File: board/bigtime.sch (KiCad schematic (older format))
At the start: 61 parts, among them IC1 NPIC6C596A, IC2 TPS62152, IC3 25AA02E48, IC4 STM32F407VET6, IC8 LDL212DR, J2 MICROUSB, P1 CONN_IN, P2 CONN_OUT, P3 +12V, P4 SWD_TC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

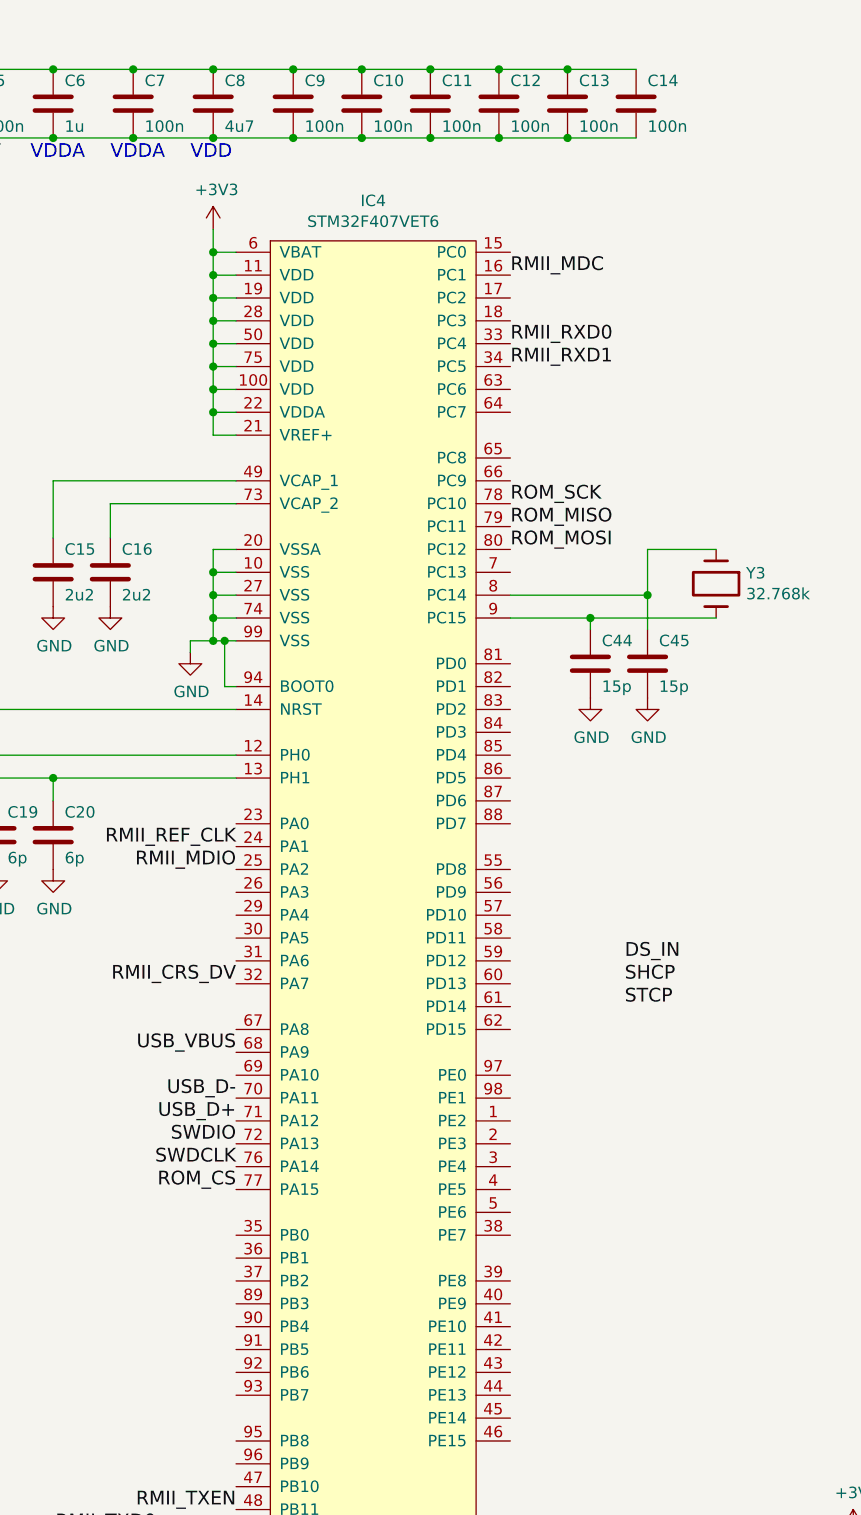
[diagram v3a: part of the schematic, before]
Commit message: nearly done first route
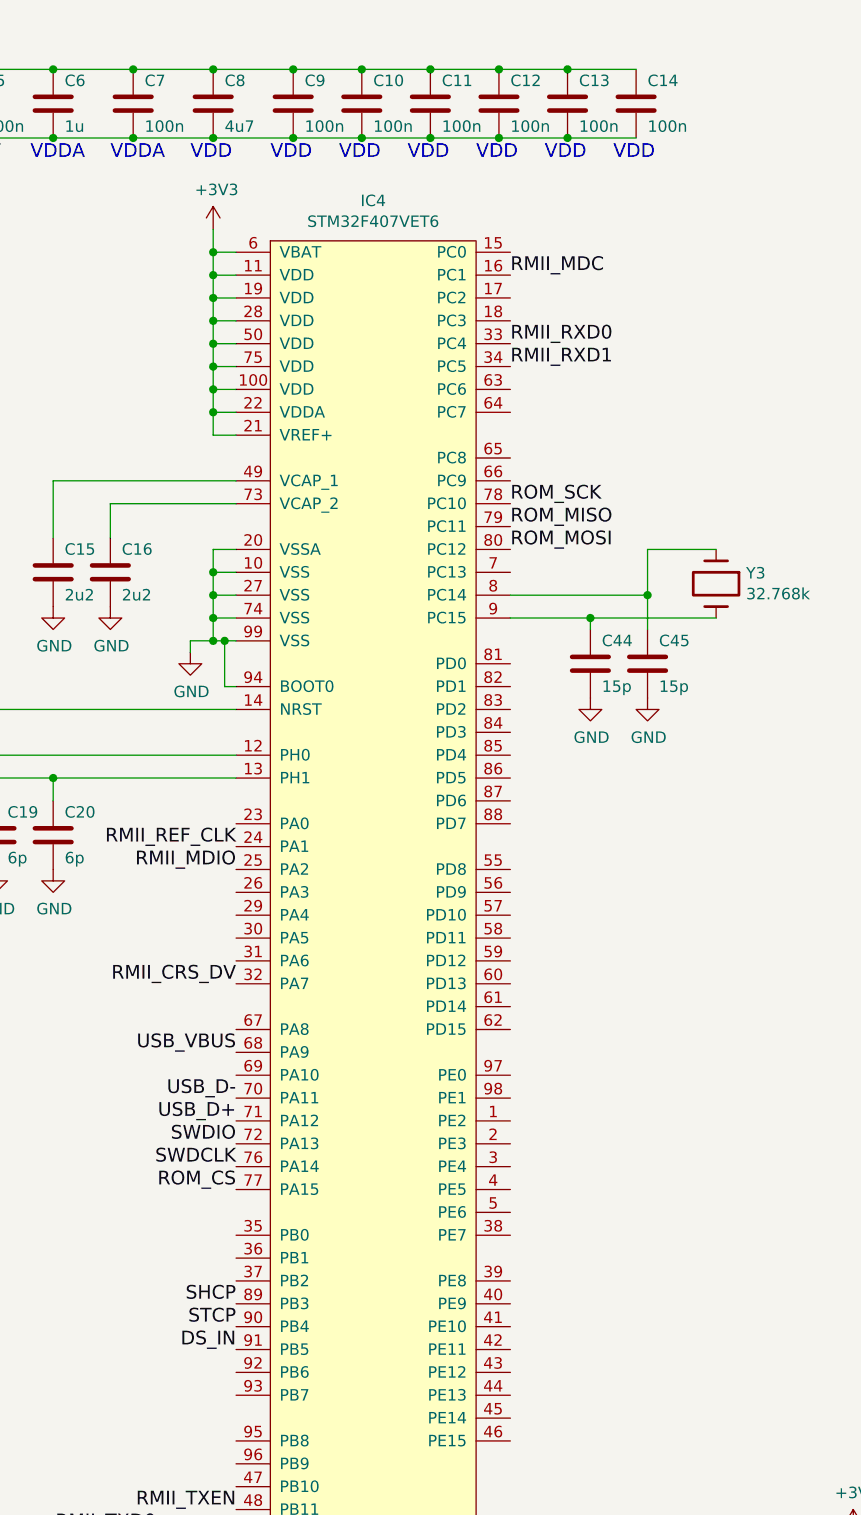
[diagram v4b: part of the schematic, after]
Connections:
- net DS_IN: now also IC4.91 (PB5)
- net SHCP: now also IC4.89 (PB3)
- net STCP: now also IC4.90 (PB4)
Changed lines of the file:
@@
 Text Label 8100 6150 2    60   ~ 0
 STCP
-Text Label 4250 4650 0    60   ~ 0
+Text Label 2550 6350 2    60   ~ 0
 DS_IN
-Text Label 4250 4750 0    60   ~ 0
+Text Label 2550 6150 2    60   ~ 0
 SHCP
-Text Label 4250 4850 0    60   ~ 0
+Text Label 2550 6250 2    60   ~ 0
 STCP
 $Comp
@@
 	1    0    0    -1
 $EndComp
+Text Notes 2700 1150 0    60   ~ 0
+VDD
+Text Notes 3000 1150 0    60   ~ 0
+VDD
+Text Notes 3300 1150 0    60   ~ 0
+VDD
+Text Notes 3600 1150 0    60   ~ 0
+VDD
+Text Notes 3900 1150 0    60   ~ 0
+VDD
+Text Notes 4200 1150 0    60   ~ 0
+VDD
 $EndSCHEMATC

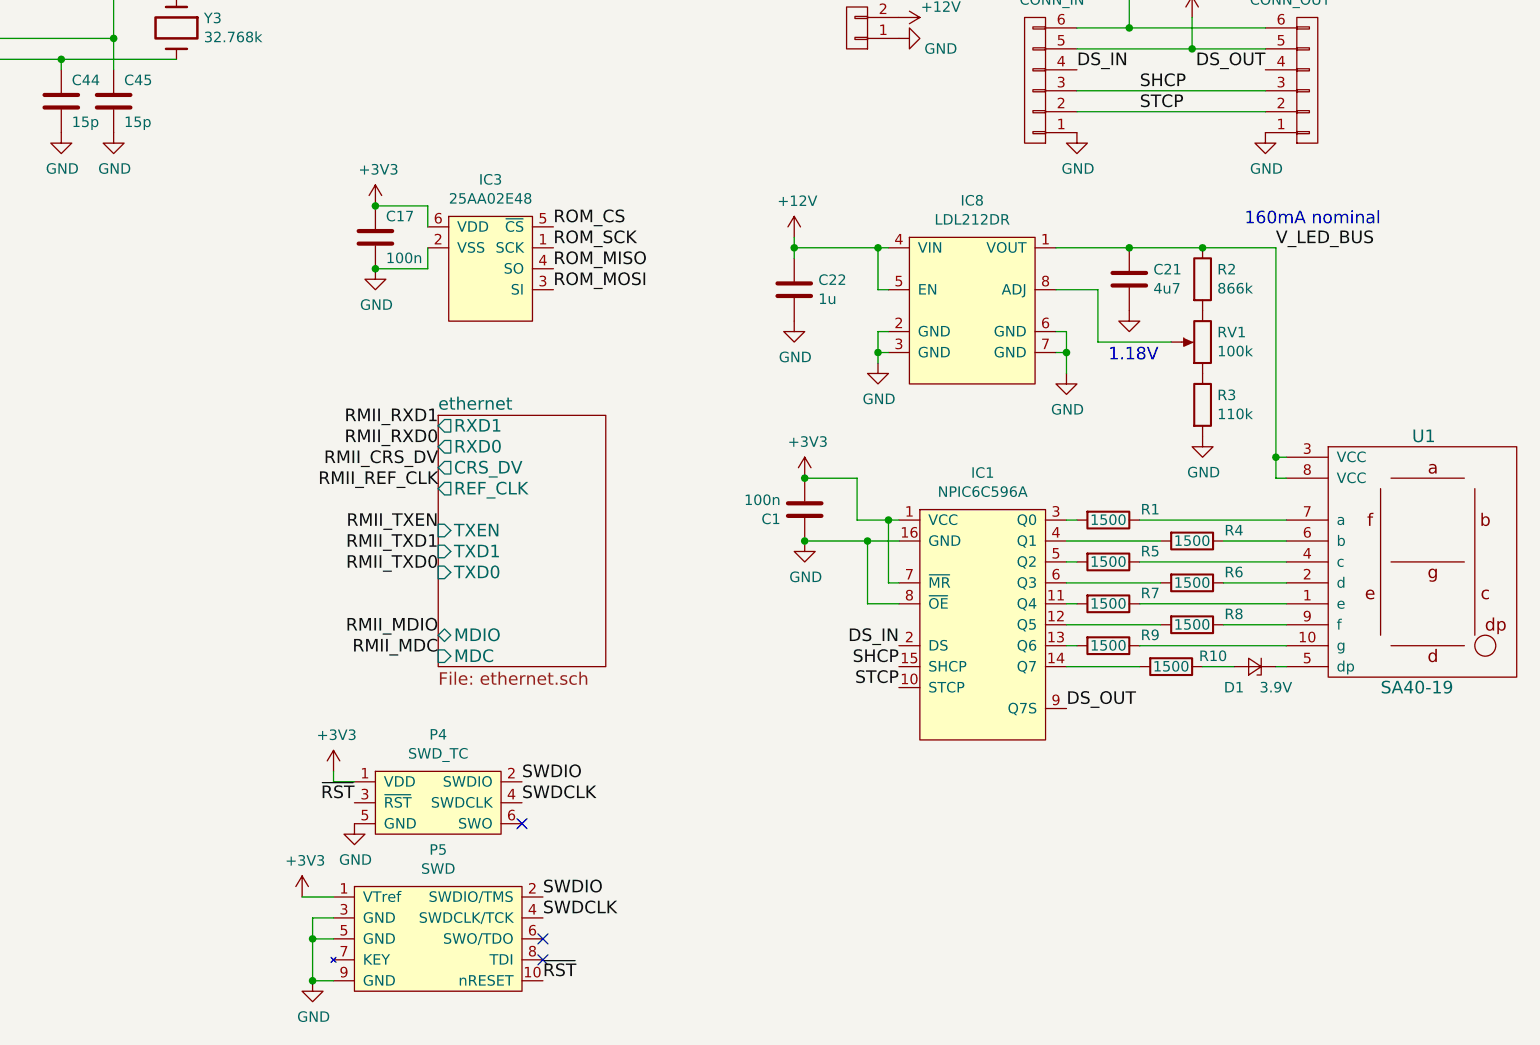
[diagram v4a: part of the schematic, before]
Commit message: Finished first (pretty awful) route
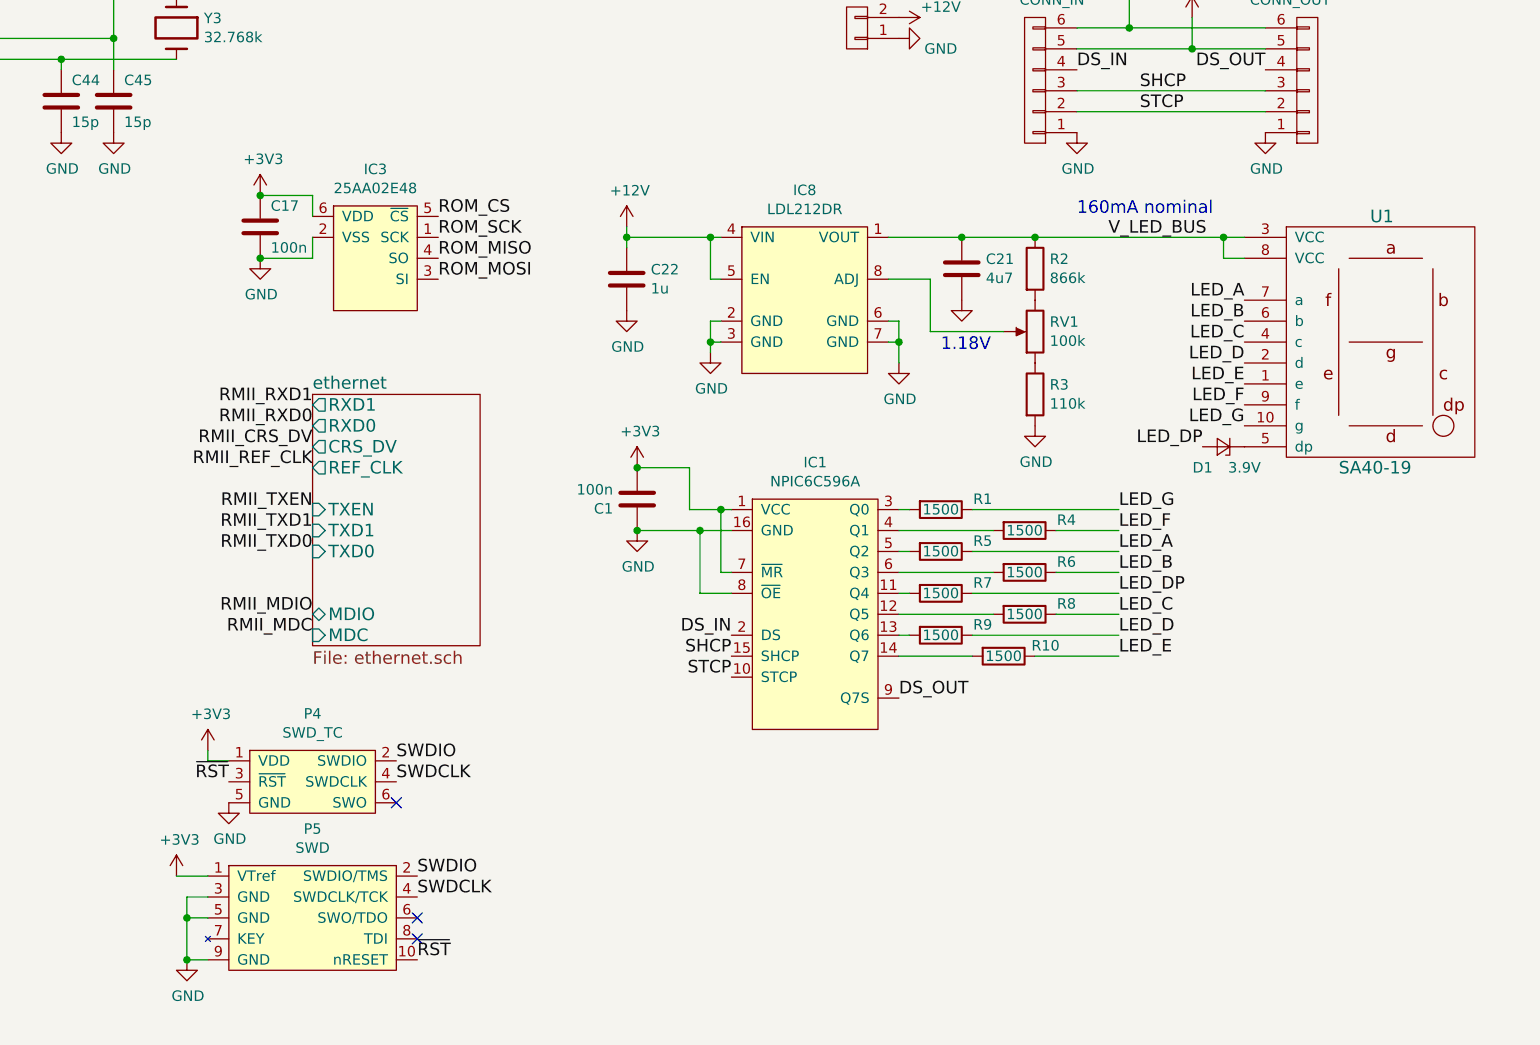
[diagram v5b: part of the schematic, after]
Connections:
- net LED_DP: now reaches R7.1
- net LED_DP: now also D1.2 (A); no longer U1.1 (e)
- net LED_D: now reaches R9.1
- net LED_D: now also U1.2 (d); no longer U1.10 (g)
- net LED_B: now reaches R6.1
- net LED_B: now also U1.6 (b); no longer U1.2 (d)
- net LED_A: now reaches R5.1
- net LED_A: now also U1.7 (a); no longer U1.4 (c)
- net LED_F: now reaches R4.1
- net LED_F: now also U1.9 (f); no longer U1.6 (b)
- net LED_G: now reaches R1.1
- net LED_G: now also U1.10 (g); no longer U1.7 (a)
- net LED_C: now reaches R8.1
- net LED_C: now also U1.4 (c); no longer U1.9 (f)
- net LED_E: now reaches R10.1
- net LED_E: now also U1.1 (e); no longer D1.2 (A)
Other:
- moved on the sheet: C1, C17, C21, C22, D1, IC1, IC3, IC8, P4, P5, R1, R10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

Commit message: Made capacitors more consistent in vals+fps
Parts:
- C4: footprint agg:0805 -> agg:0603; Farnell (none) -> 2494232
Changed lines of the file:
@@
 F 0 "C4" H 10565 1196 50  0000 L CNN
 F 1 "22u" H 10565 1105 50  0000 L CNN
-F 2 "agg:0805" H 1988 -200 50  0001 C CNN
+F 2 "agg:0603" H 1988 -200 50  0001 C CNN
 F 3 "" H 1950 -50 50  0000 C CNN
+F 4 "2494232" H 10450 1150 60  0001 C CNN "Farnell"
 	1    10450 1150
 	1    0    0    -1
